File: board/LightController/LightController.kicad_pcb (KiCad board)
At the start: 2 copper layers, 114.8 x 68.6 mm, 34 parts, among them J1 PJ-051AH, J2 Light bank 1, J3 Light Bank 2, J4 Light Bank 3, U1 CPC1002N, U10 CPC1002N, U11 CPC1002N, U12 FeatherS2, U2 CPC1002N, U3 CPC1002N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

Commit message: Add test points.
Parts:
- added TP1: 24V, TestPoint:TestPoint_Pad_D4.0mm, F.Cu at (144.0, 100.8)
- added TP2: GND, TestPoint:TestPoint_Loop_D2.54mm_Drill1.5mm_Beaded, F.Cu at (131.8, 98.3)
- added TP3: 5V, TestPoint:TestPoint_Pad_D4.0mm, F.Cu at (130.3, 63.5)
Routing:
- net +24V: track 323.7 -> 329.6 mm
- net +5V: track 26.9 -> 31.5 mm
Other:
- board text added: "Do not draw more than 5W on each pin"
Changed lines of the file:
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@@
   (net 53 "unconnected-(U12-Pad27)")
   (net 54 "unconnected-(U12-Pad28)")
+  (footprint "TestPoint:TestPoint_Pad_D4.0mm" (layer "F.Cu")
+    (at 130.302 63.5)
+    (descr "SMD pad as test Point, diameter 4.0mm")
+    (tags "test point SMD pad")
+    (property "Sheetfile" "LightController.kicad_sch")
+    (property "Sheetname" "")
+    (attr exclude_from_pos_files)
+    (fp_text reference "TP3" (at 0 -2.898) (layer "F.SilkS") hide
+      (effects (font (size 1 1) (thickness 0.15)))
+    )
+    (fp_text value "5V" (at 0 -3.556) (layer "F.SilkS")
+      (effects (font (size 1 1) (thickness 0.15)))
+    )
+    (fp_text user "${REFERENCE}" (at -0.254 -5.08) (layer "F.Fab")
+      (effects (font (size 1 1) (thickness 0.15)))
+    )
+    (fp_circle (center 0 0) (end 0 2.25) (layer "F.SilkS") (width 0.12) (fill none))
+    (fp_circle (center 0 0) (end 2.5 0) (layer "F.CrtYd") (width 0.05) (fill none))
+    (pad "1" smd circle (at 0 0) (size 4 4) (layers "F.Cu" "F.Mask")
+      (net 5 "+5V") (pinfunction "1") (pintype "passive"))
+  )
   (footprint "Resistor_SMD:R_0805_2012Metric" (layer "F.Cu")
     (at 170.942 55.118 -90)
@@
     )
   )
+  (footprint "TestPoint:TestPoint_Loop_D2.54mm_Drill1.5mm_Beaded" (layer "F.Cu")
+    (at 131.826 98.298)
+    (descr "wire loop with bead as test point, loop diameter2.548mm, hole diameter 1.5mm")
+    (tags "test point wire loop bead")
+    (property "Sheetfile" "LightController.kicad_sch")
+    (property "Sheetname" "")
+    (attr through_hole)
+    (fp_text reference "TP2" (at 0.7 2.5) (layer "F.SilkS") hide
+      (effects (font (size 1 1) (thickness 0.15)))
+    )
+    (fp_text value "GND" (at 0 -2.8) (layer "F.SilkS")
+      (effects (font (size 1 1) (thickness 0.15)))
+    )
+    (fp_text user "${REFERENCE}" (at 0.7 2.5) (layer "F.Fab")
+      (effects (font (size 1 1) (thickness 0.15)))
+    )
+    (fp_circle (center 0 0) (end 1.7 0) (layer "F.SilkS") (width 0.12) (fill none))
+    (fp_circle (center 0 0) (end 2 0) (layer "F.CrtYd") (width 0.05) (fill none))
+    (fp_line (start 1.3 -0.3) (end -1.3 -0.3) (layer "F.Fab") (width 0.12))
+    (fp_line (start -1.3 -0.3) (end -1.3 0.3) (layer "F.Fab") (width 0.12))
+    (fp_line (start 1.3 0.3) (end 1.3 -0.3) (layer "F.Fab") (width 0.12))
+    (fp_line (start -1.3 0.3) (end 1.3 0.3) (layer "F.Fab") (width 0.12))
+    (fp_circle (center 0 0) (end 1.5 0) (layer "F.Fab") (width 0.12) (fill none))
+    (pad "1" thru_hole circle (at 0 0) (size 3 3) (drill 1.5) (layers *.Cu *.Mask)
+      (net 2 "GND") (pinfunction "1") (pintype "passive"))
+    (model "${KICAD6_3DMODEL_DIR}/TestPoint.3dshapes/TestPoint_Loop_D2.54mm_Drill1.5mm_Beaded.wrl"
+      (offset (xyz 0 0 0))
+      (scale (xyz 1 1 1))
+      (rotate (xyz 0 0 0))
+    )
+  )
+  (footprint "TestPoint:TestPoint_Pad_D4.0mm" (layer "F.Cu")
+    (at 144.018 100.838)
+    (descr "SMD pad as test Point, diameter 4.0mm")
+    (tags "test point SMD pad")
+    (property "Sheetfile" "LightController.kicad_sch")
+    (property "Sheetname" "")
+    (attr exclude_from_pos_files)
+    (fp_text reference "TP1" (at 0 -2.898) (layer "F.SilkS") hide
+      (effects (font (size 1 1) (thickness 0.15)))
+    )
+    (fp_text value "24V" (at 0 3.81) (layer "F.SilkS")
+      (effects (font (size 1 1) (thickness 0.15)))
+    )
+    (fp_text user "${REFERENCE}" (at 0 -2.9) (layer "F.Fab")
+      (effects (font (size 1 1) (thickness 0.15)))
+    )
+    (fp_circle (center 0 0) (end 0 2.25) (layer "F.SilkS") (width 0.12) (fill none))
+    (fp_circle (center 0 0) (end 2.5 0) (layer "F.CrtYd") (width 0.05) (fill none))
+    (pad "1" smd circle (at 0 0) (size 4 4) (layers "F.Cu" "F.Mask")
+      (net 1 "+24V") (pinfunction "1") (pintype "passive"))
+  )
   (footprint "Package_SO:SOP-4_3.8x4.1mm_P2.54mm" (layer "F.Cu")
     (at 187.452 68.326)
@@
       (effects (font (size 1 1) (thickness 0.15)))
     )
-    (fp_text value "2x22µF" (at 77.734 39.116 90) (layer "F.Fab")
+    (fp_text value "2x22µF" (at 0.254 2.032 180) (layer "F.Fab")
       (effects (font (size 1 1) (thickness 0.15)))
     )
@@
     (effects (font (size 1.5 1.5) (thickness 0.2)))
   )
+  (gr_text "Do not draw\nmore than 5W\non each pin" (at 180.594 90.424) (layer "F.SilkS")
+    (effects (font (size 1.5 1.5) (thickness 0.3)) (justify left))
+  )
   (gr_text "GND" (at 197.612 56.134) (layer "F.SilkS")
     (effects (font (size 1 1) (thickness 0.15)) (justify right))
@@
   (segment (start 145.796 67.376) (end 149.838 67.376) (width 0.6) (layer "F.Cu") (net 1))
   (segment (start 149.882 61.192) (end 149.882 68.602) (width 2.2) (layer "F.Cu") (net 1))
+  (segment (start 144.018 100.838) (end 149.86 100.838) (width 0.25) (layer "F.Cu") (net 1))
   (segment (start 177.038 83.312) (end 166.878 83.312) (width 0.4) (layer "F.Cu") (net 1))
   (segment (start 167.894 63.754) (end 167.386 63.754) (width 0.6) (layer "F.Cu") (net 1))
@@
   (segment (start 182.88 65.532) (end 179.578 68.834) (width 0.4) (layer "F.Cu") (net 1))
   (segment (start 177.546 92.71) (end 168.402 92.71) (width 0.4) (layer "F.Cu") (net 1))
+  (segment (start 149.86 100.838) (end 149.882 100.86) (width 0.25) (layer "F.Cu") (net 1))
   (segment (start 178.772 105.874) (end 177.546 104.648) (width 0.4) (layer "F.Cu") (net 1))
   (segment (start 166.878 63.754) (end 161.798 68.834) (width 0.6) (layer "F.Cu") (net 1))
@@
   (segment (start 140.02 65.1565) (end 140.02 63.82) (width 0.6) (layer "F.Cu") (net 4))
   (segment (start 140.02 63.82) (end 139.258 63.058) (width 0.6) (layer "F.Cu") (net 4))
-  (segment (start 133.35 68.072) (end 124.206 68.072) (width 0.6) (layer "F.Cu") (net 5))
+  (segment (start 130.048 68.072) (end 124.206 68.072) (width 0.6) (layer "F.Cu") (net 5))
   (segment (start 136.652 71.374) (end 140.02 71.374) (width 0.6) (layer "F.Cu") (net 5))
   (segment (start 136.398 65.278) (end 138.5515 67.4315) (width 0.6) (layer "F.Cu") (net 5))
   (segment (start 136.398 64.0545) (end 136.398 65.278) (width 0.6) (layer "F.Cu") (net 5))
+  (segment (start 130.302 67.818) (end 130.048 68.072) (width 0.25) (layer "F.Cu") (net 5))
+  (segment (start 130.302 63.5) (end 130.302 67.818) (width 0.25) (layer "F.Cu") (net 5))
   (segment (start 140.02 71.374) (end 140.02 67.4315) (width 0.6) (layer "F.Cu") (net 5))
   (segment (start 133.35 68.072) (end 136.652 71.374) (width 0.6) (layer "F.Cu") (net 5))
+  (segment (start 133.35 68.072) (end 130.048 68.072) (width 0.6) (layer "F.Cu") (net 5))
   (segment (start 138.5515 67.4315) (end 140.02 67.4315) (width 0.6) (layer "F.Cu") (net 5))
   (segment (start 198.887 58.679) (end 199.644 58.679) (width 0.4) (layer "F.Cu") (net 6))

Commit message: Added second parallel bypass cap.
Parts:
- added C4: 22µF, Capacitor_SMD:C_0805_2012Metric, F.Cu at (141.0, 68.1)
- C3: value 2x22µF -> 22µF
- moved C2 2.41 mm to (140.2, 58.0)
- moved L1 2.41 mm to (136.4, 60.6)
- moved U5 2.41 mm to (141.0, 63.9)
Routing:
- net GND: track 26.1 -> 31.3 mm, vias 12 -> 13
- net +5V: track 31.5 -> 32.6 mm
- net +24V: track 329.6 -> 330.6 mm

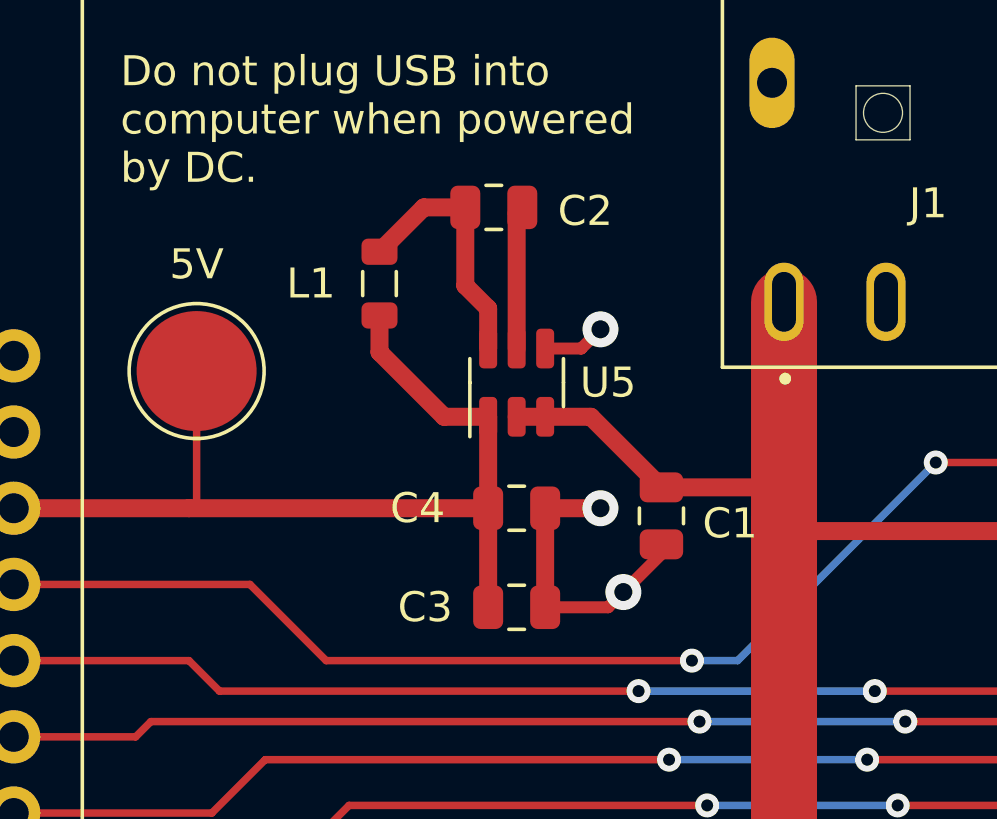
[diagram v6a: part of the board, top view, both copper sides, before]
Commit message: Increased caps to 1206.
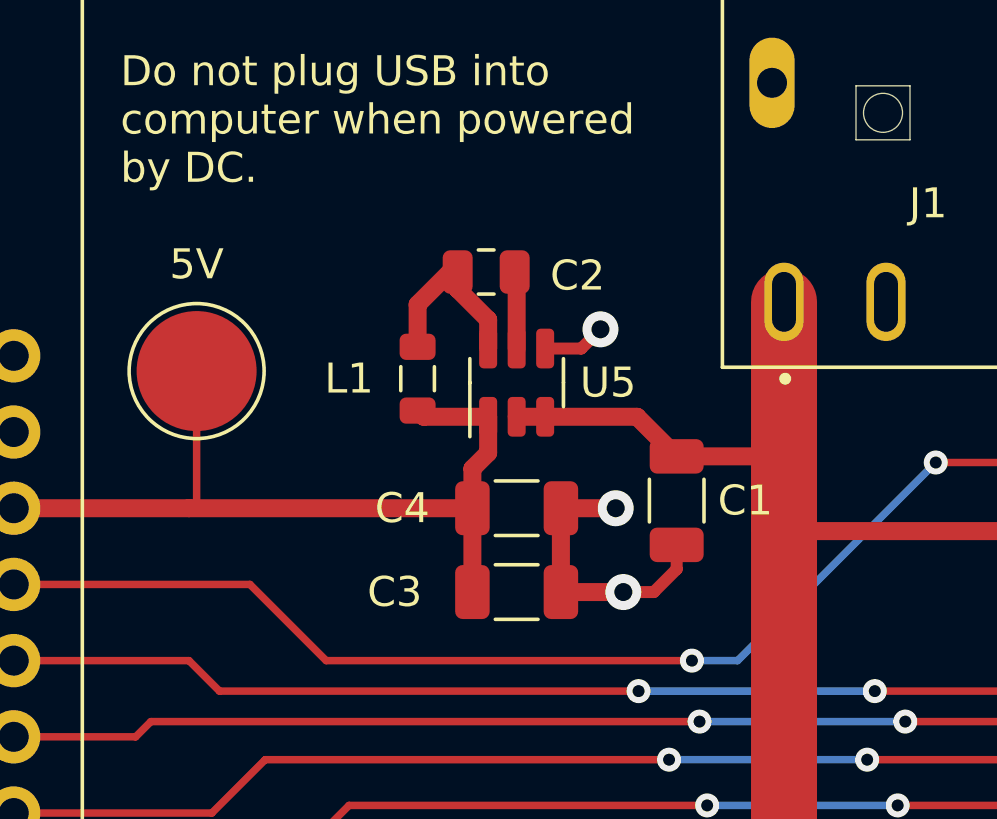
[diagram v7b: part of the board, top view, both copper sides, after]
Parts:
- C1, C3, C4: footprint Capacitor_SMD:C_0805_2012Metric -> Capacitor_SMD:C_1206_3216Metric
- L1: value 4.7µH -> 8.7µH
- moved L1 3.41 mm to (137.7, 63.8)
- moved C2 2.17 mm to (140.0, 60.2)
- moved C1 0.72 mm to (146.3, 67.8)
- moved C3 0.51 mm to (141.0, 70.9)
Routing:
- net +5V: track 32.6 -> 28.5 mm
- net Net-(C2-Pad2): track 8.49 -> 6.17 mm
- net Net-(C2-Pad1): track 4.78 -> 2.58 mm

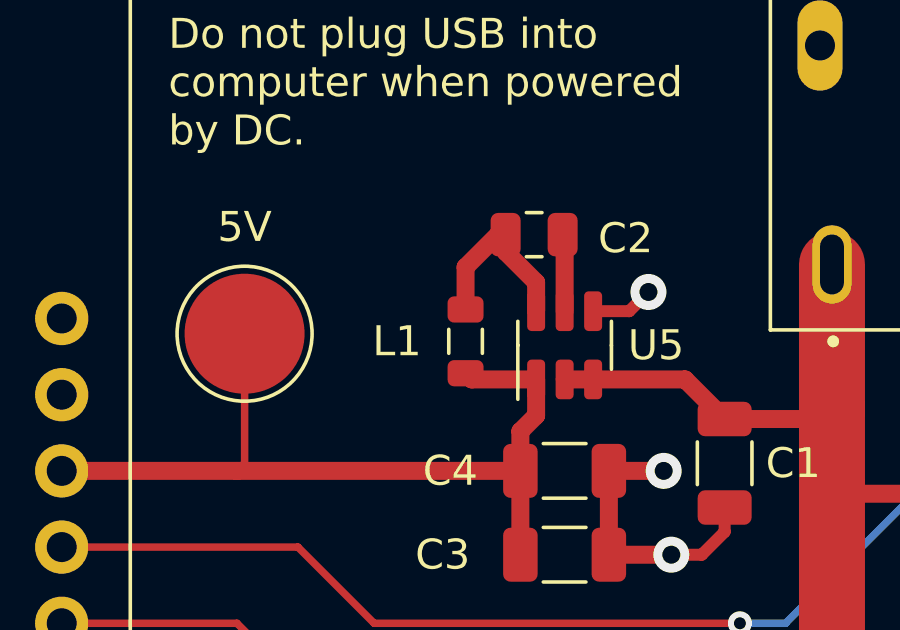
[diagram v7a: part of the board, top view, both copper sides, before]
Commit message: Increased inductor size to 1206.
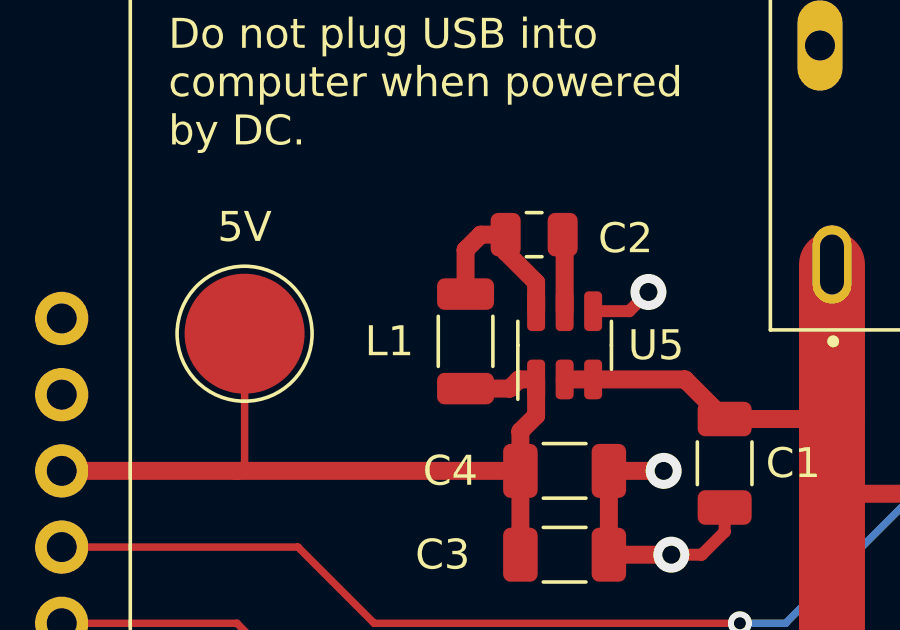
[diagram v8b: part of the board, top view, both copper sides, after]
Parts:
- L1: footprint Inductor_SMD:L_0805_2012Metric -> Inductor_SMD:L_1206_3216Metric
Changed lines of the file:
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@@
     )
   )
-  (footprint "Inductor_SMD:L_0805_2012Metric" (layer "F.Cu")
+  (footprint "Inductor_SMD:L_1206_3216Metric" (layer "F.Cu")
     (at 137.668 63.754 -90)
-    (descr "Inductor SMD 0805 (2012 Metric), square (rectangular) end terminal, IPC_7351 nominal, (Body size source: IPC-SM-782 page 80, https://www.pcb-3d.com/wordpress/wp-content/uploads/ipc-sm-782a_amendment_1_and_2.pdf), generated with kicad-footprint-generator")
+    (descr "Inductor SMD 1206 (3216 Metric), square (rectangular) end terminal, IPC_7351 nominal, (Body size source: IPC-SM-782 page 80, https://www.pcb-3d.com/wordpress/wp-content/uploads/ipc-sm-782a_amendment_1_and_2.pdf), generated with kicad-footprint-generator")
     (tags "inductor")
     (property "Sheetfile" "LightController.kicad_sch")
     (property "Sheetname" "")
     (attr smd)
-    (fp_text reference "L1" (at 0 2.286 180) (layer "F.SilkS")
-      (effects (font (size 1 1) (thickness 0.15)))
-    )
-    (fp_text value "8.7µH" (at -2.6725 1.524 180) (layer "F.Fab")
-      (effects (font (size 1 1) (thickness 0.15)))
-    )
-    (fp_text user "${REFERENCE}" (at 0 0 90) (layer "F.Fab")
-      (effects (font (size 0.5 0.5) (thickness 0.08)))
-    )
-    (fp_line (start -0.399622 -0.56) (end 0.399622 -0.56) (layer "F.SilkS") (width 0.12))
-    (fp_line (start -0.399622 0.56) (end 0.399622 0.56) (layer "F.SilkS") (width 0.12))
-    (fp_line (start 1.75 -0.85) (end 1.75 0.85) (layer "F.CrtYd") (width 0.05))
-    (fp_line (start -1.75 -0.85) (end 1.75 -0.85) (layer "F.CrtYd") (width 0.05))
-    (fp_line (start -1.75 0.85) (end -1.75 -0.85) (layer "F.CrtYd") (width 0.05))
-    (fp_line (start 1.75 0.85) (end -1.75 0.85) (layer "F.CrtYd") (width 0.05))
-    (fp_line (start -1 -0.45) (end 1 -0.45) (layer "F.Fab") (width 0.1))
-    (fp_line (start 1 0.45) (end -1 0.45) (layer "F.Fab") (width 0.1))
-    (fp_line (start -1 0.45) (end -1 -0.45) (layer "F.Fab") (width 0.1))
-    (fp_line (start 1 -0.45) (end 1 0.45) (layer "F.Fab") (width 0.1))
-    (pad "1" smd roundrect (at -1.0625 0 270) (size 0.875 1.2) (layers "F.Cu" "F.Paste" "F.Mask") (roundrect_rratio 0.25)
+    (fp_text reference "L1" (at 0 2.54) (layer "F.SilkS")
+      (effects (font (size 1 1) (thickness 0.15)))
+    )
+    (fp_text value "8.7µH" (at -2.794 3.556) (layer "F.Fab")
+      (effects (font (size 1 1) (thickness 0.15)))
+    )
+    (fp_text user "${REFERENCE}" (at 0 0 -90) (layer "F.Fab")
+      (effects (font (size 0.8 0.8) (thickness 0.12)))
+    )
+    (fp_line (start -0.835242 -0.91) (end 0.835242 -0.91) (layer "F.SilkS") (width 0.12))
+    (fp_line (start -0.835242 0.91) (end 0.835242 0.91) (layer "F.SilkS") (width 0.12))
+    (fp_line (start -2.35 -1.2) (end 2.35 -1.2) (layer "F.CrtYd") (width 0.05))
+    (fp_line (start 2.35 1.2) (end -2.35 1.2) (layer "F.CrtYd") (width 0.05))
+    (fp_line (start 2.35 -1.2) (end 2.35 1.2) (layer "F.CrtYd") (width 0.05))
+    (fp_line (start -2.35 1.2) (end -2.35 -1.2) (layer "F.CrtYd") (width 0.05))
+    (fp_line (start -1.6 0.8) (end -1.6 -0.8) (layer "F.Fab") (width 0.1))
+    (fp_line (start -1.6 -0.8) (end 1.6 -0.8) (layer "F.Fab") (width 0.1))
+    (fp_line (start 1.6 0.8) (end -1.6 0.8) (layer "F.Fab") (width 0.1))
+    (fp_line (start 1.6 -0.8) (end 1.6 0.8) (layer "F.Fab") (width 0.1))
+    (pad "1" smd roundrect (at -1.575 0 270) (size 1.05 1.9) (layers "F.Cu" "F.Paste" "F.Mask") (roundrect_rratio 0.238095)
       (net 4 "Net-(C2-Pad2)") (pinfunction "1") (pintype "passive"))
-    (pad "2" smd roundrect (at 1.0625 0 270) (size 0.875 1.2) (layers "F.Cu" "F.Paste" "F.Mask") (roundrect_rratio 0.25)
+    (pad "2" smd roundrect (at 1.575 0 270) (size 1.05 1.9) (layers "F.Cu" "F.Paste" "F.Mask") (roundrect_rratio 0.238095)
       (net 5 "+5V") (pinfunction "2") (pintype "passive"))
-    (model "${KICAD6_3DMODEL_DIR}/Inductor_SMD.3dshapes/L_0805_2012Metric.wrl"
+    (model "${KICAD6_3DMODEL_DIR}/Inductor_SMD.3dshapes/L_1206_3216Metric.wrl"
       (offset (xyz 0 0 0))
       (scale (xyz 1 1 1))
@@
   (segment (start 140.97 62.749) (end 140.97 60.264) (width 0.6) (layer "F.Cu") (net 3))
   (segment (start 140.97 60.264) (end 140.904 60.198) (width 0.6) (layer "F.Cu") (net 3))
-  (segment (start 138.75 60.198) (end 137.668 61.28) (width 0.6) (layer "F.Cu") (net 4))
-  (segment (start 137.668 62.6915) (end 137.668 61.28) (width 0.6) (layer "F.Cu") (net 4))
-  (segment (start 139.004 60.198) (end 138.75 60.198) (width 0.6) (layer "F.Cu") (net 4))
   (segment (start 139.004 60.772) (end 140.02 61.788) (width 0.6) (layer "F.Cu") (net 4))
+  (segment (start 138.176 60.198) (end 137.668 60.706) (width 0.6) (layer "F.Cu") (net 4))
   (segment (start 139.004 60.198) (end 139.004 60.772) (width 0.6) (layer "F.Cu") (net 4))
+  (segment (start 139.004 60.198) (end 138.176 60.198) (width 0.6) (layer "F.Cu") (net 4))
   (segment (start 140.02 61.788) (end 140.02 62.749) (width 0.6) (layer "F.Cu") (net 4))
-  (segment (start 137.8755 65.024) (end 137.668 64.8165) (width 0.6) (layer "F.Cu") (net 5))
+  (segment (start 137.668 60.706) (end 137.668 62.179) (width 0.6) (layer "F.Cu") (net 4))
   (segment (start 140.02 66.228) (end 139.495 66.753) (width 0.6) (layer "F.Cu") (net 5))
+  (segment (start 139.141 65.329) (end 137.668 65.329) (width 0.6) (layer "F.Cu") (net 5))
   (segment (start 130.048 68.072) (end 124.206 68.072) (width 0.6) (layer "F.Cu") (net 5))
   (segment (start 139.495 68.072) (end 130.048 68.072) (width 0.6) (layer "F.Cu") (net 5))
   (segment (start 130.302 67.818) (end 130.048 68.072) (width 0.25) (layer "F.Cu") (net 5))
   (segment (start 140.02 65.024) (end 140.02 66.228) (width 0.6) (layer "F.Cu") (net 5))
+  (segment (start 139.446 65.024) (end 139.141 65.329) (width 0.6) (layer "F.Cu") (net 5))
   (segment (start 130.302 63.5) (end 130.302 67.818) (width 0.25) (layer "F.Cu") (net 5))
-  (segment (start 140.02 65.024) (end 137.8755 65.024) (width 0.6) (layer "F.Cu") (net 5))
   (segment (start 139.495 66.753) (end 139.495 68.072) (width 0.6) (layer "F.Cu") (net 5))
+  (segment (start 140.02 65.024) (end 139.446 65.024) (width 0.6) (layer "F.Cu") (net 5))
   (segment (start 139.495 68.072) (end 139.495 70.866) (width 0.6) (layer "F.Cu") (net 5))
   (segment (start 198.887 58.679) (end 199.644 58.679) (width 0.4) (layer "F.Cu") (net 6))
